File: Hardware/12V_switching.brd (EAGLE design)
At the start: 39.4 x 50.9 mm, 10 parts, among them IC5 LM2576D2TR4-5G, J1 POWERPOLE_POWER45A, J2 POWERPOLE_POWER45A

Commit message: Fix switching regulator reference
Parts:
- IC5: value LM2576D2TR4-5G -> LM2576D2TR4-012G; device LM2576D2TR4-5G:D2TSUFFIX-CASE936A-02-ISSUEC -> LM2576:D2TSUFFIX-CASE936A-02-ISSUEC
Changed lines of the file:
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@@
 <element name="C11" library="rcl" package="UD-10X10_NICHICON" value="1000uF" x="21.59" y="40.005" rot="R90"/>
 <element name="D2" library="diode" package="DO-214AC" value="SAC32" x="21.59" y="23.495"/>
-<element name="IC5" library="LM2576D2TR4-5G" package="D2TSUFFIX-CASE936A-02-ISSUEC" value="LM2576D2TR4-5G" x="6.985" y="25.4">
-<attribute name="MOUSER_PART_NUMBER" value="863-LM2576D2TR4-5G" x="6.985" y="25.4" size="1.778" layer="27" display="off"/>
+<element name="IC5" library="LM2576" package="D2TSUFFIX-CASE936A-02-ISSUEC" value="LM2576D2TR4-012G" x="6.985" y="25.4">
+<attribute name="MOUSER_PART_NUMBER" value="863-LM2576D2TR4-012G" x="6.985" y="25.4" size="1.778" layer="27" display="off"/>
 <attribute name="MANUFACTURER_NAME" value="ON Semiconductor" x="6.985" y="25.4" size="1.778" layer="27" display="off"/>
 <attribute name="MOUSER_PRICE-STOCK" value="https://www.mouser.com/Search/Refine.aspx?Keyword=863-LM2576D2TR4-5G" x="6.985" y="25.4" size="1.778" layer="27" display="off"/>
 <attribute name="HEIGHT" value="mm" x="6.985" y="25.4" size="1.778" layer="27" display="off"/>
-<attribute name="MANUFACTURER_PART_NUMBER" value="LM2576D2TR4-5G" x="6.985" y="25.4" size="1.778" layer="27" display="off"/>
+<attribute name="MANUFACTURER_PART_NUMBER" value="LM2576D2TR4-012G " x="6.985" y="25.4" size="1.778" layer="27" display="off"/>
 <attribute name="DESCRIPTION" value="Voltage Regulators - Switching Regulators 5V 3A Buck PWM" x="6.985" y="25.4" size="1.778" layer="27" display="off"/>
+<attribute name="MPN" value="LM2576D2TR4-012G " x="6.985" y="25.4" size="1.778" layer="27" display="off"/>
 </element>
 <element name="L1" library="MSS1583-104KEB" package="INDPM150150X860N" value="MSS1583-104KEB" x="8.255" y="41.275" rot="R90">

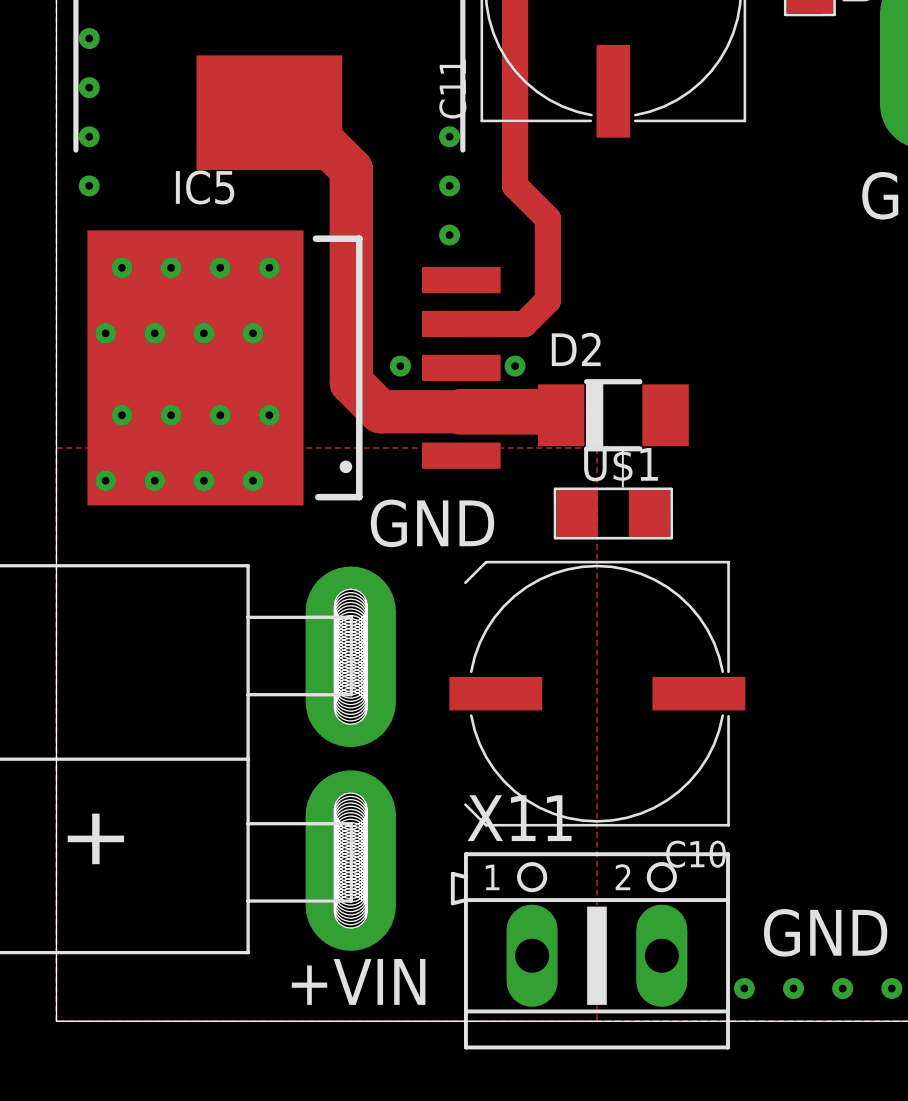
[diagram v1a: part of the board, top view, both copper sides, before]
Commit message: Trace optimisation around the FTDI chip
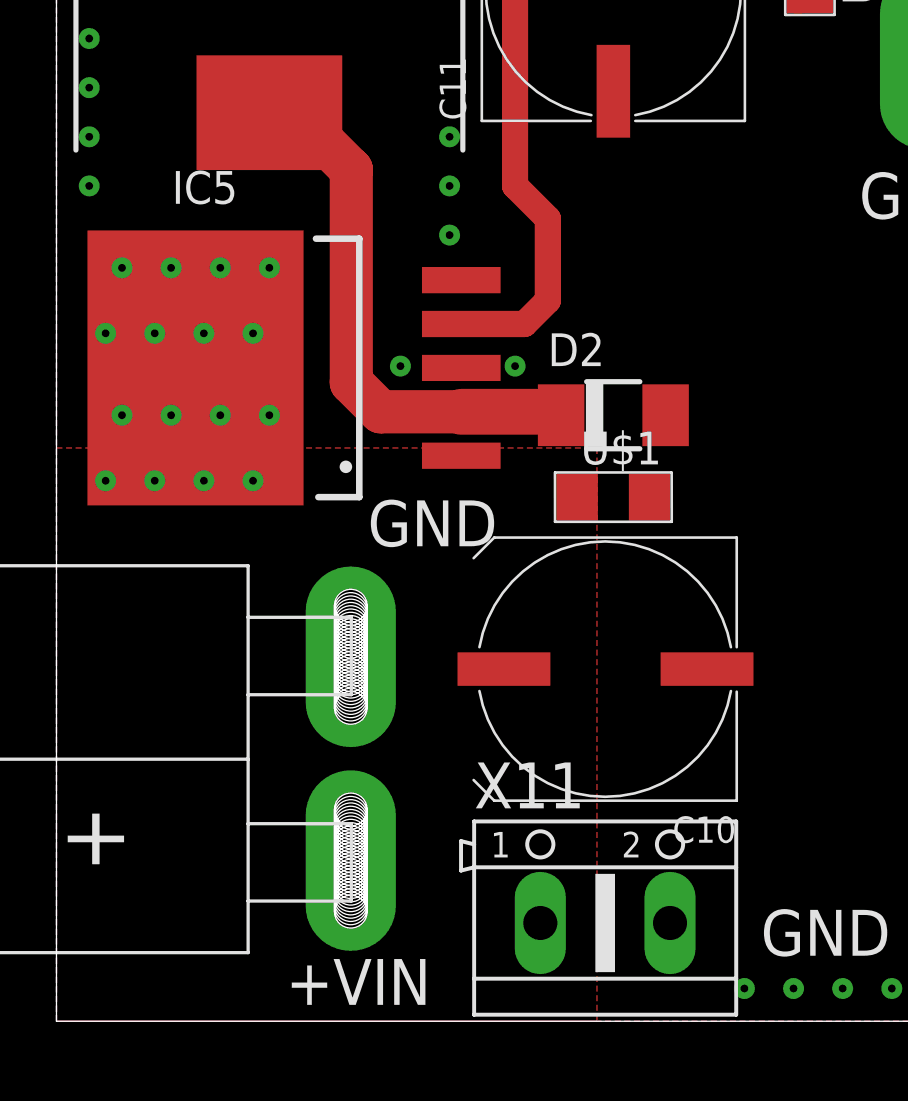
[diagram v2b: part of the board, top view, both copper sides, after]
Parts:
- IC5: device LM2576:D2TSUFFIX-CASE936A-02-ISSUEC -> LM2576:TO263-5
- moved X11 1.31 mm to (21.3, 3.81)
- moved C10 1.00 mm to (21.3, 13.7)
- moved U$1 0.64 mm to (21.6, 20.3)
- turned IC5 to 90 degrees
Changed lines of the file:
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@@
 <setting verticaltext="up"/>
 </settings>
-<grid distance="0.635" unitdist="mm" unit="mm" style="lines" multiple="1" display="yes" altdistance="0.127" altunitdist="mm" altunit="mm"/>
+<grid distance="0.3175" unitdist="mm" unit="mm" style="lines" multiple="1" display="yes" altdistance="0.127" altunitdist="mm" altunit="mm"/>
 <layers>
 <layer number="1" name="Top" color="4" fill="1" visible="yes" active="yes"/>
@@
 <layer number="220" name="220bmp" color="21" fill="1" visible="no" active="no"/>
 <layer number="221" name="221bmp" color="22" fill="1" visible="no" active="no"/>
-<layer number="222" name="222bmp" color="23" fill="1" visible="no" active="no"/>
 <layer number="223" name="223bmp" color="24" fill="1" visible="no" active="no"/>
 <layer number="224" name="224bmp" color="25" fill="1" visible="no" active="no"/>
@@
 </autorouter>
 <elements>
-<element name="C10" library="rcl" package="UD-10X10_NICHICON" value="100uF" x="20.955" y="12.7" rot="R180"/>
+<element name="C10" library="rcl" package="UD-10X10_NICHICON" value="100uF" x="21.2725" y="13.6525" rot="R180"/>
 <element name="C11" library="rcl" package="UD-10X10_NICHICON" value="1000uF" x="21.59" y="40.005" rot="R90"/>
 <element name="D2" library="diode" package="DO-214AC" value="SAC32" x="21.59" y="23.495"/>
-<element name="IC5" library="LM2576" package="D2TSUFFIX-CASE936A-02-ISSUEC" value="LM2576D2TR4-012G" x="6.985" y="25.4">
-<attribute name="MOUSER_PART_NUMBER" value="863-LM2576D2TR4-012G" x="6.985" y="25.4" size="1.778" layer="27" display="off"/>
-<attribute name="MANUFACTURER_NAME" value="ON Semiconductor" x="6.985" y="25.4" size="1.778" layer="27" display="off"/>
-<attribute name="MOUSER_PRICE-STOCK" value="https://www.mouser.com/Search/Refine.aspx?Keyword=863-LM2576D2TR4-5G" x="6.985" y="25.4" size="1.778" layer="27" display="off"/>
-<attribute name="HEIGHT" value="mm" x="6.985" y="25.4" size="1.778" layer="27" display="off"/>
-<attribute name="MANUFACTURER_PART_NUMBER" value="LM2576D2TR4-012G " x="6.985" y="25.4" size="1.778" layer="27" display="off"/>
-<attribute name="DESCRIPTION" value="Voltage Regulators - Switching Regulators 5V 3A Buck PWM" x="6.985" y="25.4" size="1.778" layer="27" display="off"/>
-<attribute name="MPN" value="LM2576D2TR4-012G " x="6.985" y="25.4" size="1.778" layer="27" display="off"/>
+<element name="IC5" library="LM2576" package="TO263-5" value="LM2576D2TR4-012G" x="6.985" y="25.4" rot="R90">
+<attribute name="MOUSER_PART_NUMBER" value="863-LM2576D2TR4-012G" x="6.985" y="25.4" size="1.778" layer="27" rot="R90" display="off"/>
+<attribute name="MANUFACTURER_NAME" value="ON Semiconductor" x="6.985" y="25.4" size="1.778" layer="27" rot="R90" display="off"/>
+<attribute name="MOUSER_PRICE-STOCK" value="https://www.mouser.com/Search/Refine.aspx?Keyword=863-LM2576D2TR4-5G" x="6.985" y="25.4" size="1.778" layer="27" rot="R90" display="off"/>
+<attribute name="HEIGHT" value="mm" x="6.985" y="25.4" size="1.778" layer="27" rot="R90" display="off"/>
+<attribute name="MANUFACTURER_PART_NUMBER" value="LM2576D2TR4-012G " x="6.985" y="25.4" size="1.778" layer="27" rot="R90" display="off"/>
+<attribute name="DESCRIPTION" value="Voltage Regulators - Switching Regulators 5V 3A Buck PWM" x="6.985" y="25.4" size="1.778" layer="27" rot="R90" display="off"/>
+<attribute name="MPN" value="LM2576D2TR4-012G " x="6.985" y="25.4" size="1.778" layer="27" rot="R90" display="off"/>
 </element>
 <element name="L1" library="MSS1583-104KEB" package="INDPM150150X860N" value="MSS1583-104KEB" x="8.255" y="41.275" rot="R90">
@@
 <attribute name="DESCRIPTION" value="Fixed Inductors MSS1583 SMT Power 0.103Ohms 100uH" x="8.255" y="41.275" size="1.778" layer="27" rot="R90" display="off"/>
 </element>
-<element name="U$1" library="rti" package="C1206" value="47uF" x="21.59" y="19.685"/>
+<element name="U$1" library="rti" package="C1206" value="47uF" x="21.59" y="20.32"/>
 <element name="U$2" library="rti" package="C1206" value="47uF" x="29.21" y="41.275" rot="R270"/>
 <element name="J1" library="powerpoles" package="POWERPOLE_PAIR_45A" value="POWERPOLE_POWER45A" x="11.43" y="10.16" rot="R90"/>
 <element name="J2" library="powerpoles" package="POWERPOLE_PAIR_45A" value="POWERPOLE_POWER45A" x="33.655" y="41.275" rot="R270"/>
-<element name="X11" library="con-ptr500" package="AK500/2" value="" x="20.955" y="2.54">
-<attribute name="OC_NEWARK" value="unknown" x="20.955" y="2.54" size="1.778" layer="27" display="off"/>
-<attribute name="MPN" value="" x="20.955" y="2.54" size="1.778" layer="27" display="off"/>
-<attribute name="MF" value="" x="20.955" y="2.54" size="1.778" layer="27" display="off"/>
-<attribute name="OC_FARNELL" value="unknown" x="20.955" y="2.54" size="1.778" layer="27" display="off"/>
+<element name="X11" library="con-ptr500" package="AK500/2" value="" x="21.2725" y="3.81">
+<attribute name="OC_NEWARK" value="unknown" x="21.2725" y="3.81" size="1.778" layer="27" display="off"/>
+<attribute name="MPN" value="" x="21.2725" y="3.81" size="1.778" layer="27" display="off"/>
+<attribute name="MF" value="" x="21.2725" y="3.81" size="1.778" layer="27" display="off"/>
+<attribute name="OC_FARNELL" value="unknown" x="21.2725" y="3.81" size="1.778" layer="27" display="off"/>
 </element>
 </elements>
